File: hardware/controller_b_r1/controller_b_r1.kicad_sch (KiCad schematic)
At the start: 56 parts

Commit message: Added templates for new board outlines (type B rev 1), completed most of controller_b_r1 schematic and moved onto the layout.
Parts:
- added C119: 100n, Capacitor_SMD:C_0402_1005Metric, symbol Device:C_Small
- added H101, H102: MountingHole, rave_shades:M1.4 Mounting Hole, symbol Mechanical:MountingHole_Pad
- added JP101: SolderJumper_2_Open, Jumper:SolderJumper-2_P1.3mm_Open_TrianglePad1.0x1.5mm, symbol Jumper:SolderJumper_2_Open
- added R111: 100k, Resistor_SMD:R_0402_1005Metric, symbol Device:R_Small
- added SW102: Button 2, Button_Switch_SMD:SW_SPST_EVQP7A, symbol rave_shades:SW_MEC_5G
- C101, C102, C103, C104, C105, C106, C107, C108, C109, C110, C111, C112, C113, C114, C115, C116, C117, C118, C120, C121: renamed from C?; footprint (none) -> Capacitor_SMD:C_0402_1005Metric
- D101, D102, D103: renamed from D?; value Vdrop 220mV Imax 500mA -> Polarity Protection; footprint (none) -> Diode_SMD:D_0402_1005Metric; Item Link https://www.digikey.com.au/en/products/detail/central-semic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 -> https://www.digikey.com.au/en/products/detail/diodes-incorp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
- J101: renamed from J?; value 8-pin FPC Connector -> Front Pannel Connector; footprint (none) -> rave_shades:CF35082D0RE-NH; symbol Connector_Generic:Conn_01x08 -> rave_shades:Conn_01x08; Item Link https://www.digikey.com.au/en/products/detail/molex/5052780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 -> https://www.digikey.com.au/en/products/detail/cvilux-usa/CF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
- J102: renamed from J?; value 2x5 Mini SWD Header -> SWD Header; footprint (none) -> Connector_PinHeader_1.27mm:PinHeader_2x05_P1.27mm_Vertical_SMD; Item Link https://au.mouser.com/ProductDetail/Adafruit/4048?qs=vLWxof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 -> https://www.digikey.com.au/en/products/detail/adafruit-indu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
- J103: renamed from J?; value USB_B_Mini -> USB Micro B; footprint (none) -> rave_shades:USB_Micro-B_Amphenol_10118192_Horizontal; symbol Connector:USB_B_Mini -> Connector:USB_B_Micro; Item Link (none) -> https://www.digikey.com.au/en/products/detail/amphenol-cs-f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
- JP102, JP103, JP104, JP105, JP106, JP107: renamed from JP?; footprint (none) -> Jumper:SolderJumper-2_P1.3mm_Open_TrianglePad1.0x1.5mm
- MK101: renamed from MK?; footprint Sensor_Audio:Knowles_LGA-5_3.5x2.65mm -> rave_shades:SPK0641HT4H-1
- Q101: renamed from Q?; value Q_Dual_NMOS_S1G1D2S2G2D1 -> NMOS; footprint (none) -> Package_TO_SOT_SMD:SOT-363_SC-70-6; Item Link (none) -> https://www.digikey.com.au/en/products/detail/toshiba-semic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
- R101: renamed from R?; value 100k -> 10k; footprint (none) -> Resistor_SMD:R_0402_1005Metric
- R102, R103, R104, R105, R106, R107, R108, R109, R110, R112: renamed from R?; footprint (none) -> Resistor_SMD:R_0402_1005Metric
- RN101: renamed from RN?; value R_Pack04_Split -> 10k; footprint (none) -> Resistor_SMD:R_Array_Convex_4x0402; Item Link (none) -> https://www.digikey.com.au/en/products/detail/panasonic-ele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
- SW101: renamed from SW?; value SW_MEC_5G -> Button 1; footprint (none) -> Button_Switch_SMD:SW_SPST_EVQP7A; symbol Switch:SW_MEC_5G -> rave_shades:SW_MEC_5G; Item Link (none) -> https://www.digikey.com.au/en/products/detail/panasonic-ele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
- U101: renamed from U?; footprint Package_DFN_QFN:OnSemi_XDFN4-1EP_1.0x1.0mm_EP0.52x0.52mm -> Package_TO_SOT_SMD:TSOT-23-5
- U102: renamed from U?; value 74LVC2T45DC -> 74LVC2T45HK3; Item Link (none) -> https://www.digikey.com.au/en/products/detail/diodes-incorp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
- U104: renamed from U?; footprint (none) -> Package_SON:WSON-8-1EP_6x5mm_P1.27mm_EP3.4x4.3mm
- Y101: renamed from Y?; footprint (none) -> rave_shades:ECS-120-10-36B2-CWY-TR
- gave numbers to parts that had none: 1
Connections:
- net +3V3: now also R101.2, U102.1 (VCCA), R111.2; no longer R102.1, U102.8 (VCCB)
- net +5V: now also U102.8 (VCCB); no longer U102.1 (VCCA)
- net GND: now also R102.1, C119.2, H101.1, H102.1, SW102.1 (Pin_1); no longer MK101.6 (GND), MK101.7 (GND), MK101.8 (GND), R101.2, SW101.2 (A)
- net LED_CLK_3V3: now also U102.2 (1A); no longer U102.7 (1B)
- net LED_CLK_5V0: now also U102.7 (1B); no longer U102.2 (1A)
- net LED_MOSI_3V3: now also U102.3 (2A); no longer U102.6 (2B)
- net LED_MOSI_5V0: now also U102.6 (2B); no longer U102.3 (2A)
- net nRESET_SW: now also SW101.2 (Pin_2); no longer SW101.3 (B), SW101.4 (B)
- net at JP104.2 (B), JP105.1 (A), R104.1: now also JP101.1 (A)
- net USER_BUTTON_1: now reaches U103.17 (GPIO14)
- net USER_BUTTON_1: now also C119.1, R111.1, SW102.2 (Pin_2)
- net USER_BUTTON_2: now reaches U103.18 (GPIO15)
- net USER_BUTTON_2: now also JP101.2 (B)
- no-connect marks 1 -> 14
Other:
- moved on the sheet: R101, R102

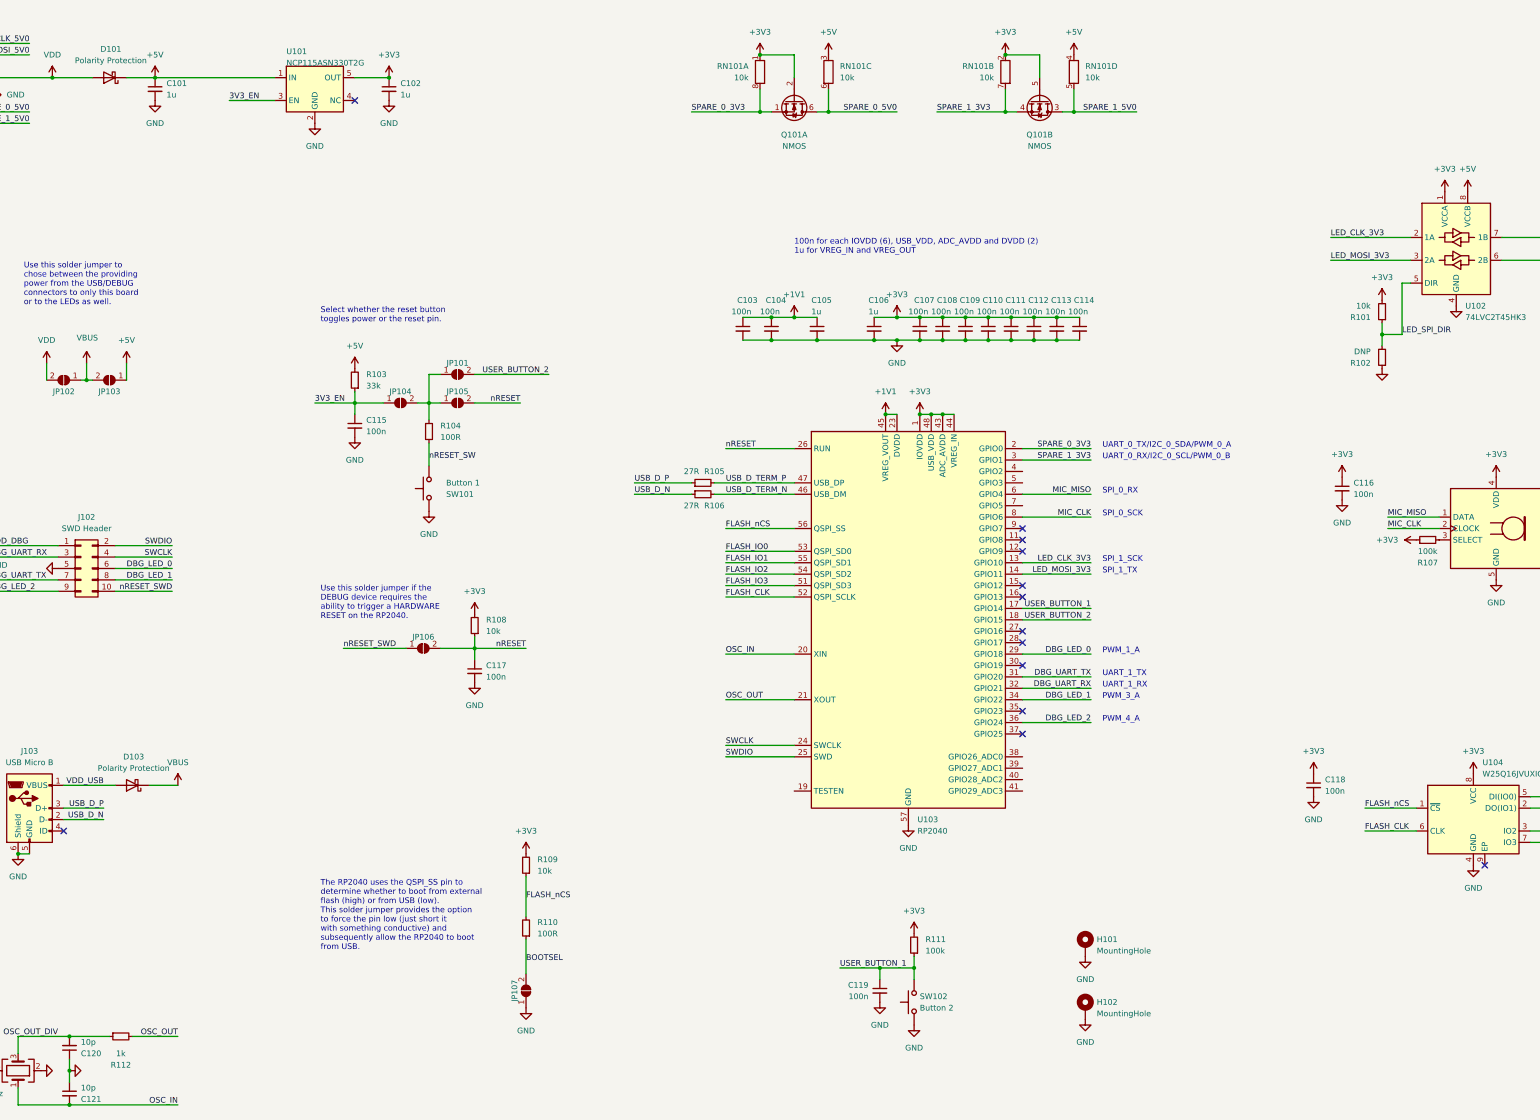
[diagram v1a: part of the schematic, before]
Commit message: Refined schematic and layout:
- Removed some caps from the user buttons, mcu reset and power reg enable because datasheets/example designs didn't have them (hopefully I don't regret it).
- Removed pullups from the user buttons because I can use the RP2040 GPIO internal pullups.
- Changed a few res values to simplify the BOM.
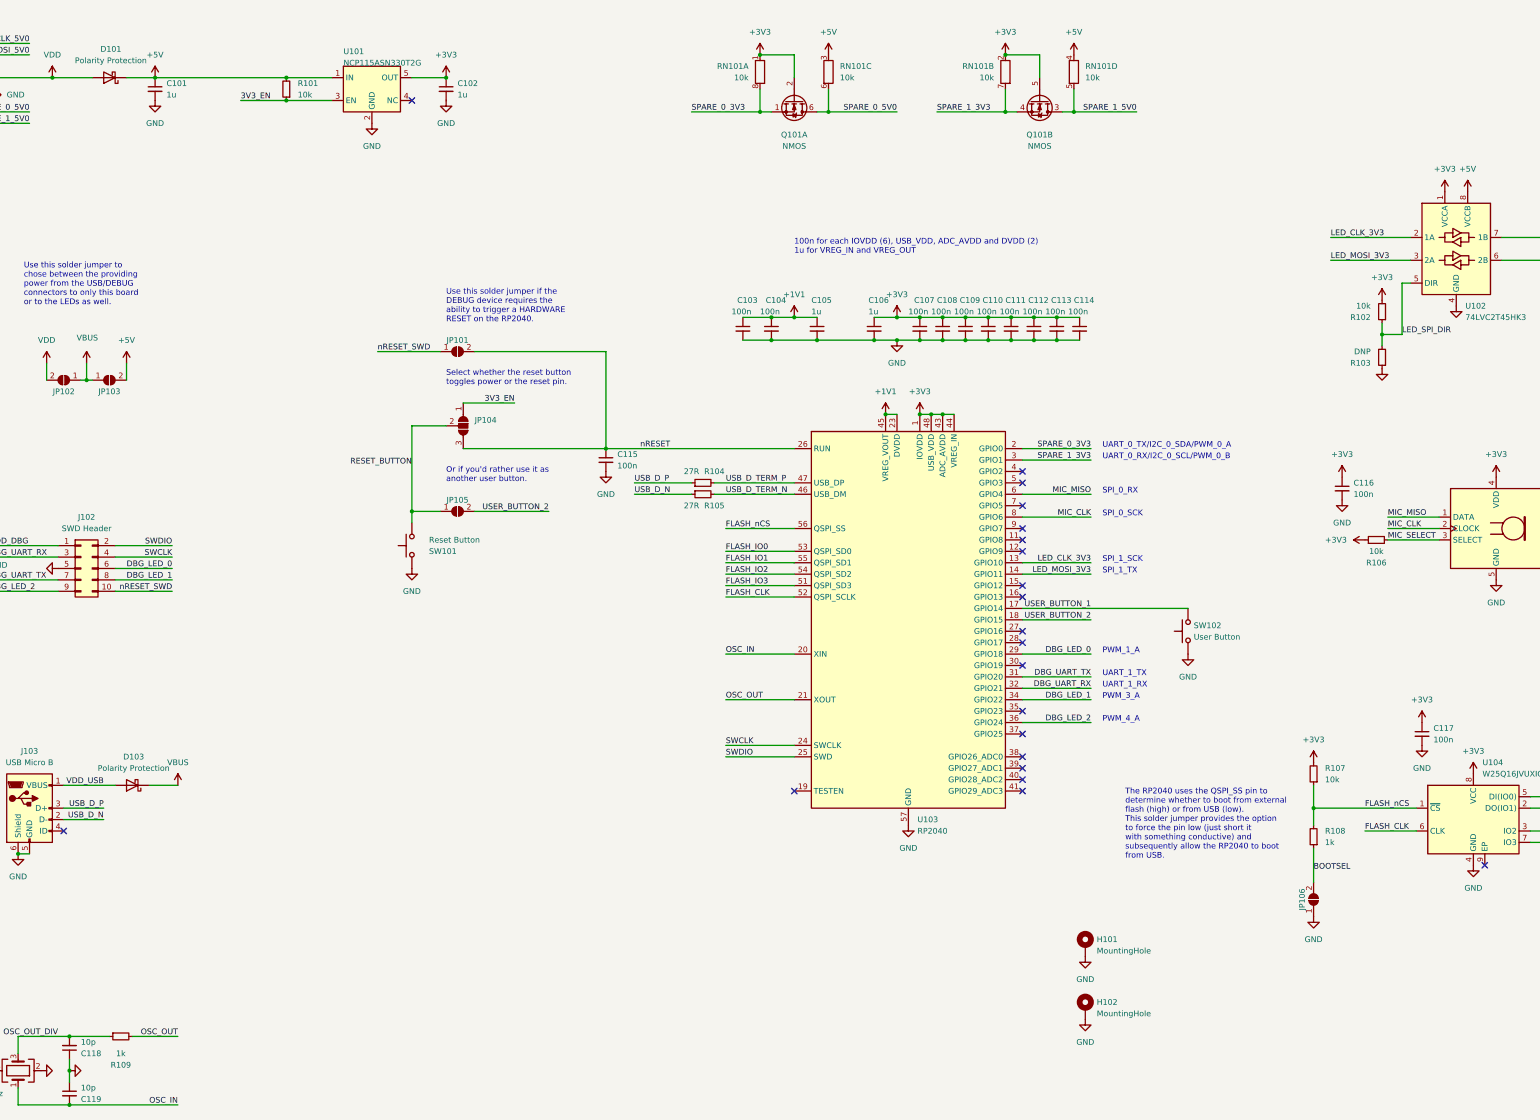
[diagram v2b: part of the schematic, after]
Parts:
- removed C117, C119: 100n, Capacitor_SMD:C_0402_1005Metric, symbol Device:C_Small
- removed JP104, JP105: SolderJumper_2_Open, Jumper:SolderJumper-2_P1.3mm_Open_TrianglePad1.0x1.5mm, symbol Jumper:SolderJumper_2_Open
- removed R104: 100R, Resistor_SMD:R_0402_1005Metric, symbol Device:R_Small
- removed R108: 10k, Resistor_SMD:R_0402_1005Metric, symbol Device:R_Small
- removed R111: 100k, Resistor_SMD:R_0402_1005Metric, symbol Device:R_Small
- added JP104: SolderJumper_3_Open, Jumper:SolderJumper-3_P1.3mm_Open_RoundedPad1.0x1.5mm, symbol Jumper:SolderJumper_3_Open
- R101: renamed from R103; value 33k -> 10k
- R106: renamed from R107; value 100k -> 10k
- R108: renamed from R110; value 100R -> 1k
- SW101: value Button 1 -> Reset Button
- SW102: value Button 2 -> User Button
- renumbered C118 to C117, C120 to C118, C121 to C119, JP106 to JP101, JP101 to JP105, JP107 to JP106, R101 to R102, R102 to R103, R105 to R104, R106 to R105, R109 to R107, R112 to R109
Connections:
- net nRESET_SW is gone; now on net RESET_BUTTON: SW101.2 (Pin_2)
- net +5V: now also JP103.2 (B); no longer JP103.1 (A)
- net 3V3_EN: now also JP104.1 (A); no longer C115.1
- net VBUS: now also JP103.1 (A); no longer JP103.2 (B)
- net nRESET: now also C115.1, JP104.3 (B)
- net RESET_BUTTON: now reaches JP105.1 (A)
- net RESET_BUTTON: now also JP104.2 (C)
- net MIC_SELECT: now reaches MK101.3 (SELECT), R106.2
- no-connect marks 14 -> 22
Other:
- note added: "Or if you'd rather use it as another user button."
- moved on the sheet: C102, C117, JP101, JP103, JP105, JP106, R101, R106, R107, R108, SW101, SW102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

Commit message: Controller board is pretty much done. USB impedance will need to be tweaked and DRC checks done once a PCB fab is decided on. Having all the serial interfaces routed from the same side (the top) of the MCU was a pain, will have to keep an eye out for EMI problems. Also restricting the board to 2 layers was probably not worth all the extra routing effort.
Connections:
- net DBG_LED_0: now also U103.27 (GPIO16); no longer U103.29 (GPIO18)
- net DBG_LED_1: now also U103.28 (GPIO17); no longer U103.34 (GPIO22)
- net DBG_LED_2: now also U103.29 (GPIO18); no longer U103.36 (GPIO24)
- net GND: now also J101.9 (NC)
- net LED_CLK_3V3: now also U102.3 (2A); no longer U102.2 (1A)
- net LED_CLK_5V0: now also U102.6 (2B); no longer U102.7 (1B)
- net LED_MOSI_3V3: now also U102.2 (1A); no longer U102.3 (2A)
- net LED_MOSI_5V0: now also U102.7 (1B); no longer U102.6 (2B)
- net USER_BUTTON_1: now also U103.15 (GPIO12); no longer U103.17 (GPIO14)
- net USER_BUTTON_2: now also U103.16 (GPIO13); no longer U103.18 (GPIO15)
- no-connect marks 22 -> 21
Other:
- moved on the sheet: SW102

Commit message: Display board layout is now 95% complete, the number of caps on the board might need some further tweaking and there are also some gaps where a few more LEDs could fit. Additionally I've decided to provide the option to use the hinges as the ground connection allowing more +5V channels on the FFC connectors which should mean more current carrying capacity. The new power board schematic has had some changes, namely the vreg has changed and so have some of the passives around it, more input protect has been added, a MOV for over voltage protection and an NMOS for reverse pol. Looking at the new vreg the power dissipation before it cooks itself (~1.1W) isn't great but it's enough for about 2.5A (at around 93% eff.) for the LEDs which hasn't usually been the bottleneck (looking at you 9V batteries). This means we're expecting around 1.8A peak input current at a Vin of 7V and need to size the fuze around that as much more current and the vreg is cooked. Might look into a over voltage shutout circuit if it seems like we're blowing fuses too often.
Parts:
- added JP107: SolderJumper_3_Open, Jumper:SolderJumper-3_P1.3mm_Open_Pad1.0x1.5mm, symbol Jumper:SolderJumper_3_Open
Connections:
- net GND: now also JP107.3 (B); no longer J101.3 (Pin_3), J101.6 (Pin_6)
- net LED_CLK_3V3: now also U102.2 (1A); no longer U102.3 (2A)
- net LED_CLK_5V0: now also J101.2 (Pin_2), U102.7 (1B); no longer J101.1 (Pin_1), U102.6 (2B)
- net LED_MOSI_3V3: now also U102.3 (2A); no longer U102.2 (1A)
- net LED_MOSI_5V0: now also J101.1 (Pin_1), U102.6 (2B); no longer J101.2 (Pin_2), U102.7 (1B)
- net VDD: now also JP107.1 (A)
- new net VDD_OR_GND: J101.3 (Pin_3), J101.6 (Pin_6), JP107.2 (C)
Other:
- note added: "Use this solder jumper to chose between using the cable to carry the return current or rely soley on the hinges. Might be useful when driving the display using the debug/usb power."
- moved on the sheet: H101, H102
